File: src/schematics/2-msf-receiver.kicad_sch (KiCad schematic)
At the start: 3 parts

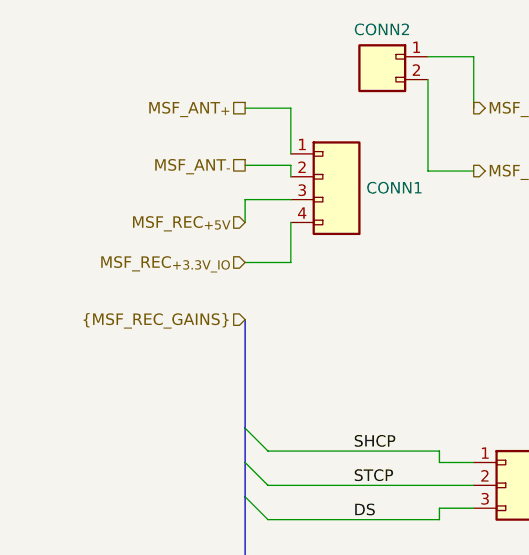
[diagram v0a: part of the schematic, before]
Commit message: Elaboration of the top-level schematicd.
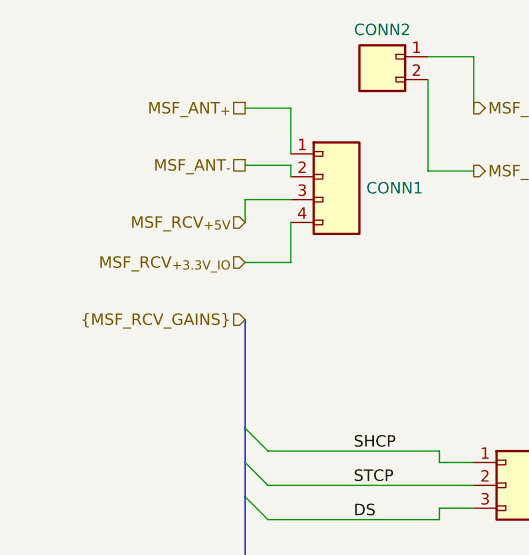
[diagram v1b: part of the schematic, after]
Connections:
- net MSF_REC_{+3.3V_IO} renamed MSF_RCV_{+3.3V_IO}
- net MSF_REC_{+5V} renamed MSF_RCV_{+5V}
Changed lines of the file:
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@@
     (company "Pete Restall <pete@restall.net>")
   )
-  (bus_alias "MSF_REC_GAINS" (members "SHCP" "STCP" "DS"))
+  (bus_alias "MSF_RCV_GAINS" (members "SHCP" "STCP" "DS"))
   (bus_entry (at 38.1 93.98) (size 2.54 2.54)
     (stroke (width 0) (type default))
@@
     (effects (font (size 1.27 1.27)) (justify right))
   )
-  (hierarchical_label "MSF_REC_{+5V}" (shape input) (at 38.1 63.5 180) (fields_autoplaced)
+  (hierarchical_label "MSF_RCV_{+5V}" (shape input) (at 38.1 63.5 180) (fields_autoplaced)
     (effects (font (size 1.27 1.27)) (justify right))
   )
-  (hierarchical_label "MSF_REC_{+3.3V_IO}" (shape input) (at 38.1 67.945 180) (fields_autoplaced)
+  (hierarchical_label "MSF_RCV_{+3.3V_IO}" (shape input) (at 38.1 67.945 180) (fields_autoplaced)
     (effects (font (size 1.27 1.27)) (justify right))
   )
@@
     (effects (font (size 1.27 1.27)) (justify left))
   )
-  (hierarchical_label "{MSF_REC_GAINS}" (shape input) (at 38.1 74.295 180) (fields_autoplaced)
+  (hierarchical_label "{MSF_RCV_GAINS}" (shape input) (at 38.1 74.295 180) (fields_autoplaced)
     (effects (font (size 1.27 1.27)) (justify right))
   )

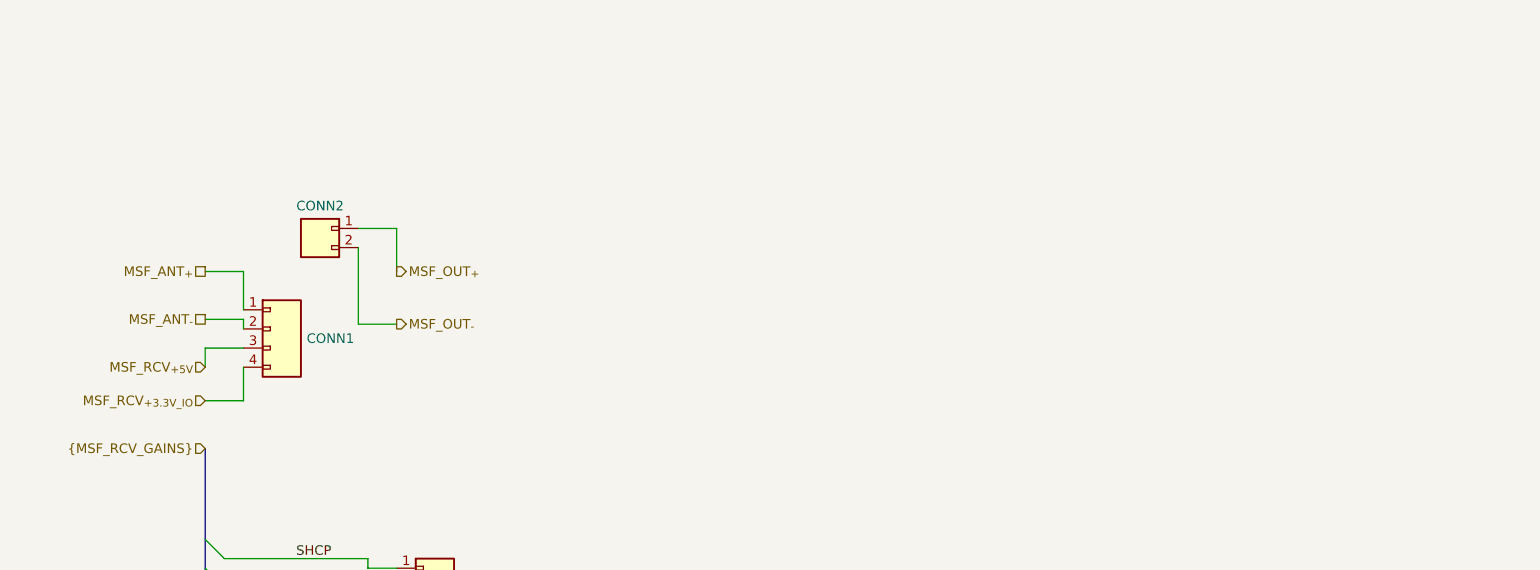
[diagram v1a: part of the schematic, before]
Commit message: Further elaboration of the design and schematics, mainly power supply calculations.
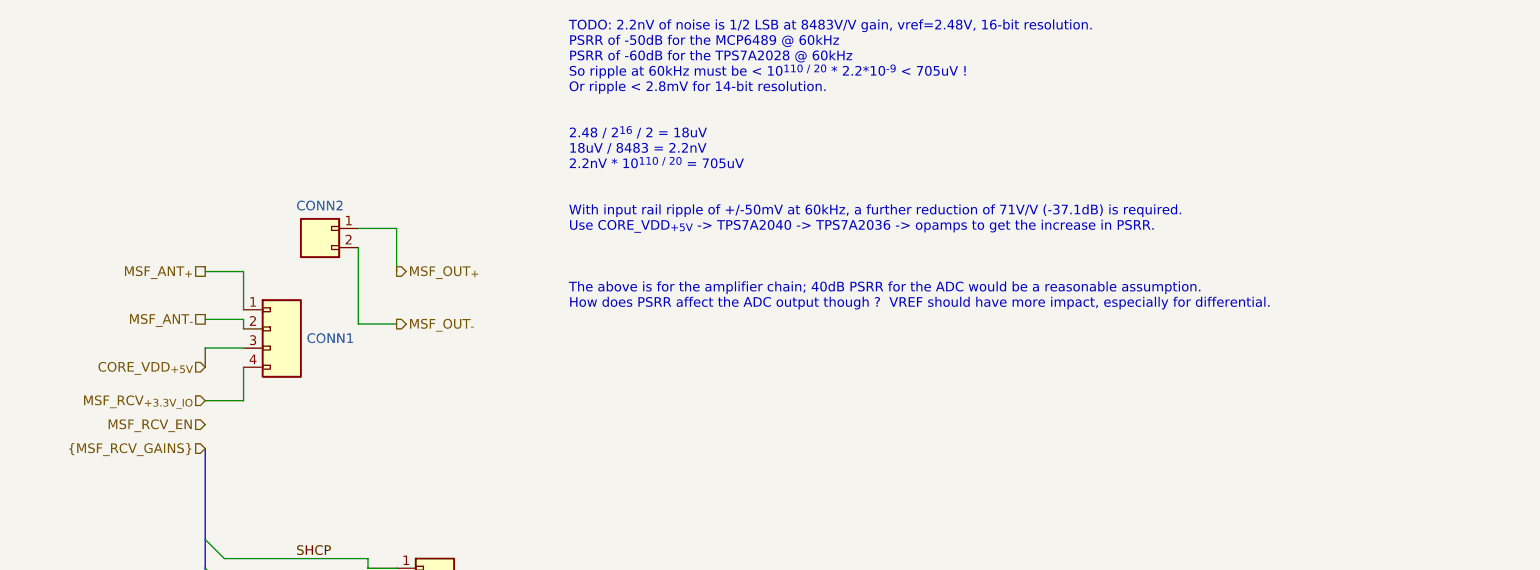
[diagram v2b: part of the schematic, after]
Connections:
- net MSF_RCV_{+5V} renamed CORE_VDD_{+5V}
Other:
- note added: "TODO: 2.2nV of noise is 1/2 LSB at 8483V/V gain, vref=2.48V, 16-bit resolution. PSRR of -50dB for the MCP6489 @ 60kHz PSRR of -60dB for the TPS7A2028 @ 60kHz So ripple at 60kHz must be < 10^{110 / 20} * 2.2*10^{-9} < 705uV ! Or ripple < 2.8mV for 14-bit resolution. 2.48 / 2^{16} / 2 = 18uV 18uV / 8483 = 2.2nV 2.2nV * 10^{110 / 20} = 705uV With input rail ripple of +/-50mV at 60kHz, a further redu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"
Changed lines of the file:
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@@
     (stroke (width 0) (type default))
+  )
+  (text "TODO: 2.2nV of noise is 1/2 LSB at 8483V/V gain, vref=2.48V, 16-bit resolution.\nPSRR of -50dB for the MCP6489 @ 60kHz\nPSRR of -60dB for the TPS7A2028 @ 60kHz\nSo ripple at 60kHz must be < 10^{110 / 20} * 2.2*10^{-9} < 705uV !\nOr ripple < 2.8mV for 14-bit resolution.\n\n\n2.48 / 2^{16} / 2 = 18uV\n18uV / 8483 = 2.2nV\n2.2nV * 10^{110 / 20} = 705uV\n\n\nWith input rail ripple of +/-50mV at 60kHz, a further reduction of 71V/V (-37.1dB) is required.\nUse CORE_VDD_{+5V} -> TPS7A2040 -> TPS7A2036 -> opamps to get the increase in PSRR.\n\n\n\nThe above is for the amplifier chain; 40dB PSRR for the ADC would be a reasonable assumption.\nHow does PSRR affect the ADC output though ?  VREF should have more impact, especially for differential."
+    (at 86.36 55.88 0)
+    (effects (font (size 1.27 1.27)) (justify left bottom))
   )
   (label "STCP" (at 50.165 92.71 0) (fields_autoplaced)
@@
     (effects (font (size 1.27 1.27)) (justify right))
   )
-  (hierarchical_label "MSF_RCV_{+5V}" (shape input) (at 38.1 63.5 180) (fields_autoplaced)
+  (hierarchical_label "CORE_VDD_{+5V}" (shape input) (at 38.1 63.5 180) (fields_autoplaced)
     (effects (font (size 1.27 1.27)) (justify right))
   )
@@
     (effects (font (size 1.27 1.27)) (justify right))
   )
+  (hierarchical_label "MSF_RCV_EN" (shape input) (at 38.1 71.12 180) (fields_autoplaced)
+    (effects (font (size 1.27 1.27)) (justify right))
+  )

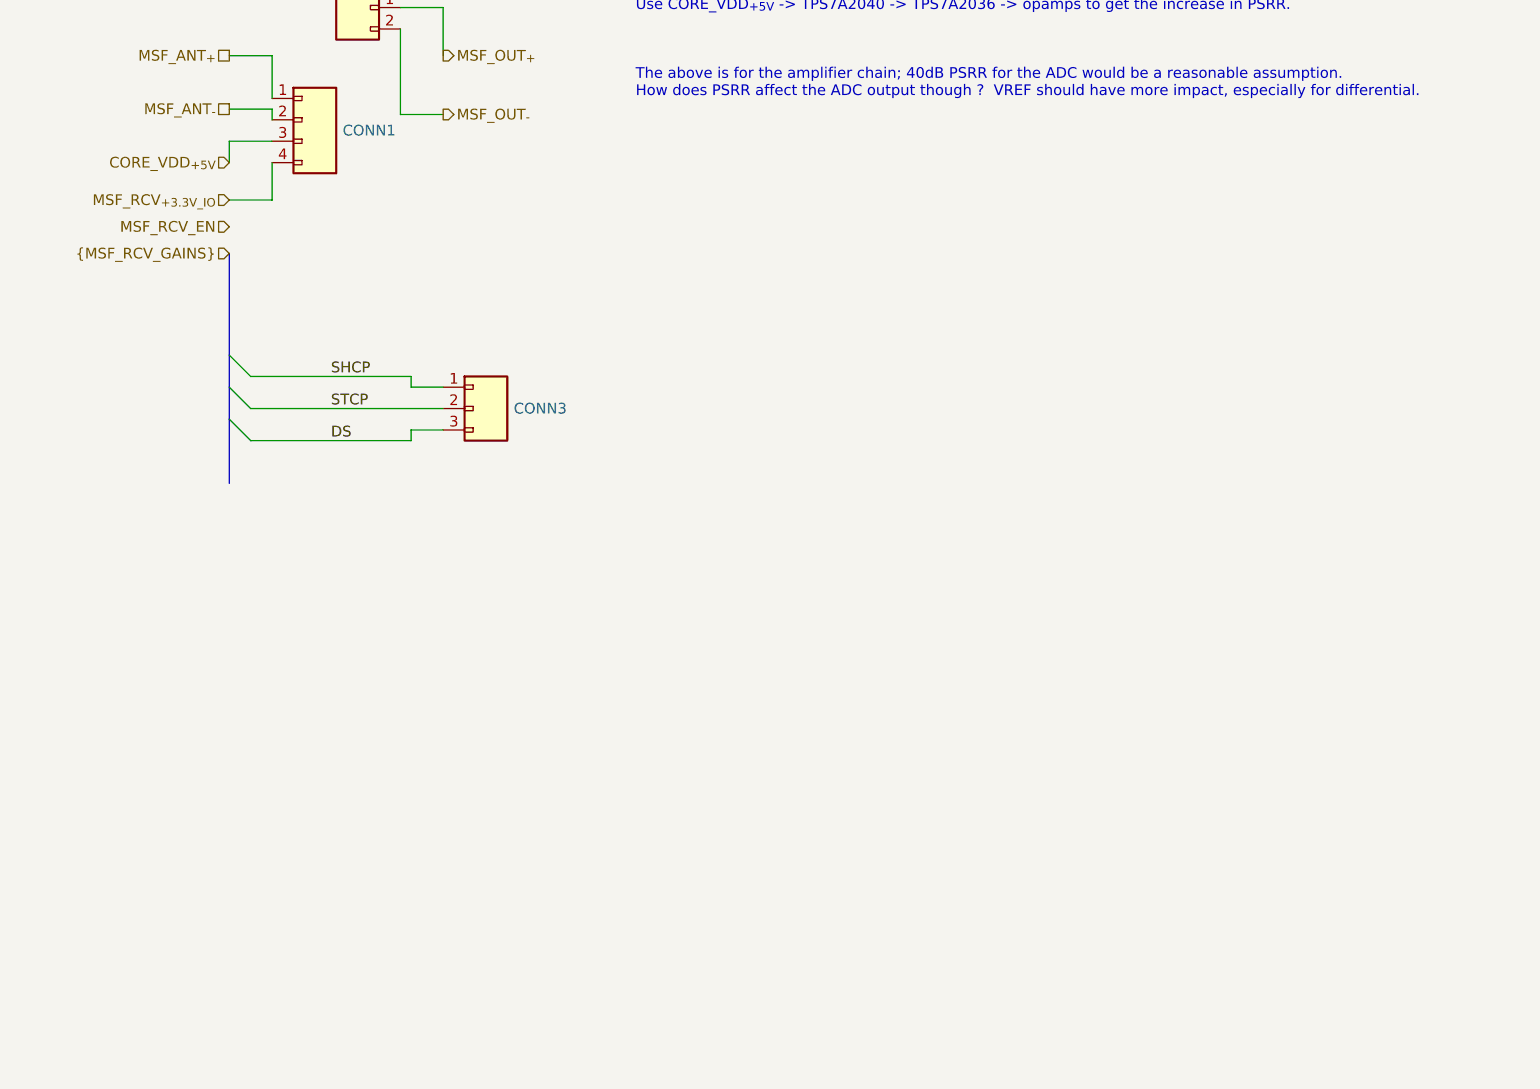
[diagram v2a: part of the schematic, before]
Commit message: Further elaboration of the USB / Power schematic.
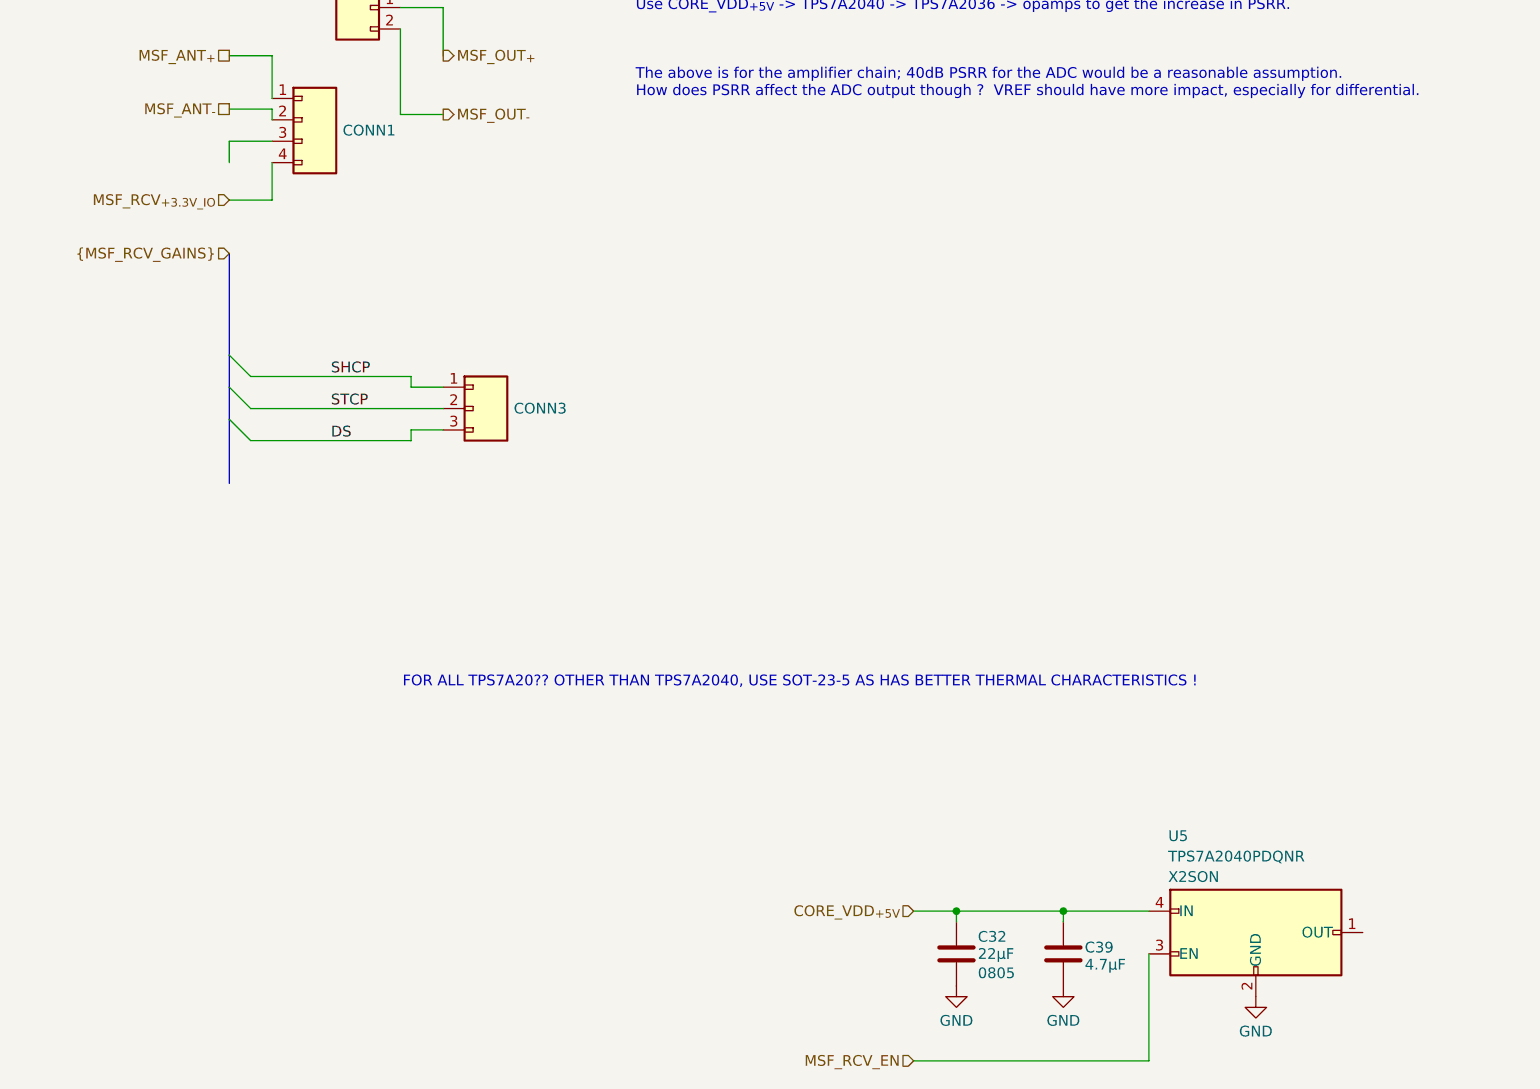
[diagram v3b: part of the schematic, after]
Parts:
- added C32: 22μF, restall-generic-capacitors:unpolarised-nominal-0805-2012, symbol restall-generic-capacitors:capacitor-unpolarised
- added C39: 4.7μF, restall-generic-capacitors:unpolarised-nominal-0402-1005, symbol restall-generic-capacitors:capacitor-unpolarised
- added U5: TPS7A2040PDQNR, restall-manufacturer-ti:X2SON4-1x1mm-0.65mm-expad-0.48x0.48mm, symbol restall-manufacturer-ti:TPS7A20??PDQNR
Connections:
- net CORE_VDD_{+5V}: now also C32.1, C39.1, U5.4 (IN); no longer CONN1.3 (P3)
- net MSF_RCV_EN: now also U5.3 (EN)
- new net GND: C32.2, C39.2, U5.2 (GND), U5.5 (GND)
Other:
- note added: "FOR ALL TPS7A20?? OTHER THAN TPS7A2040, USE SOT-23-5 AS HAS BETTER THERMAL CHARACTERISTICS !"

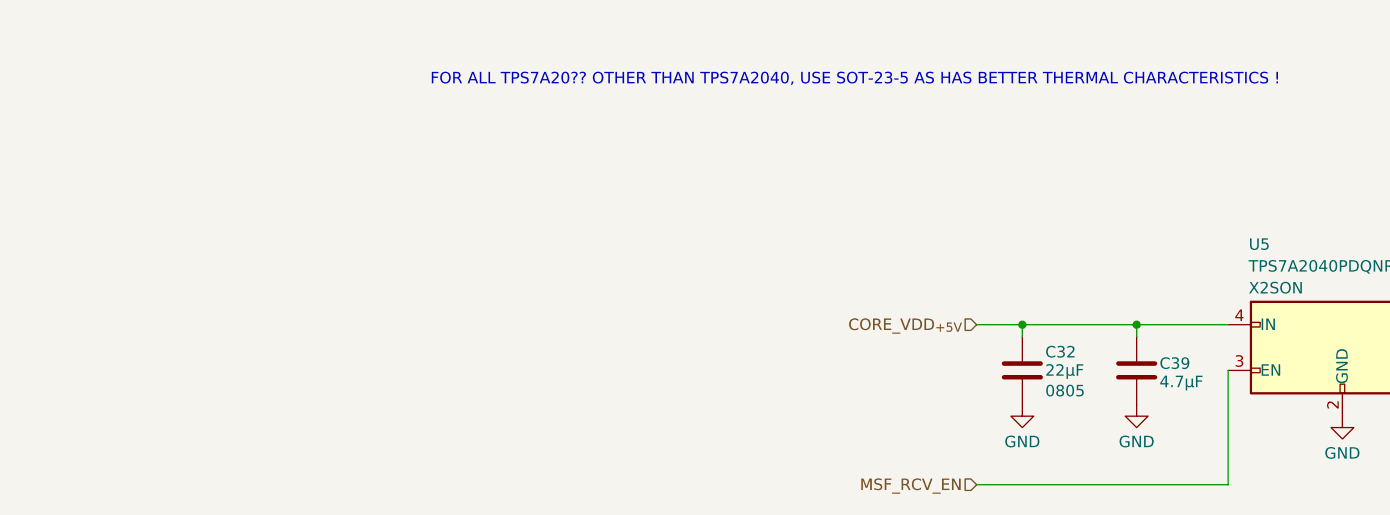
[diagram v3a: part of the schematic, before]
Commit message: Further elaboration of the USB / power module schematics.
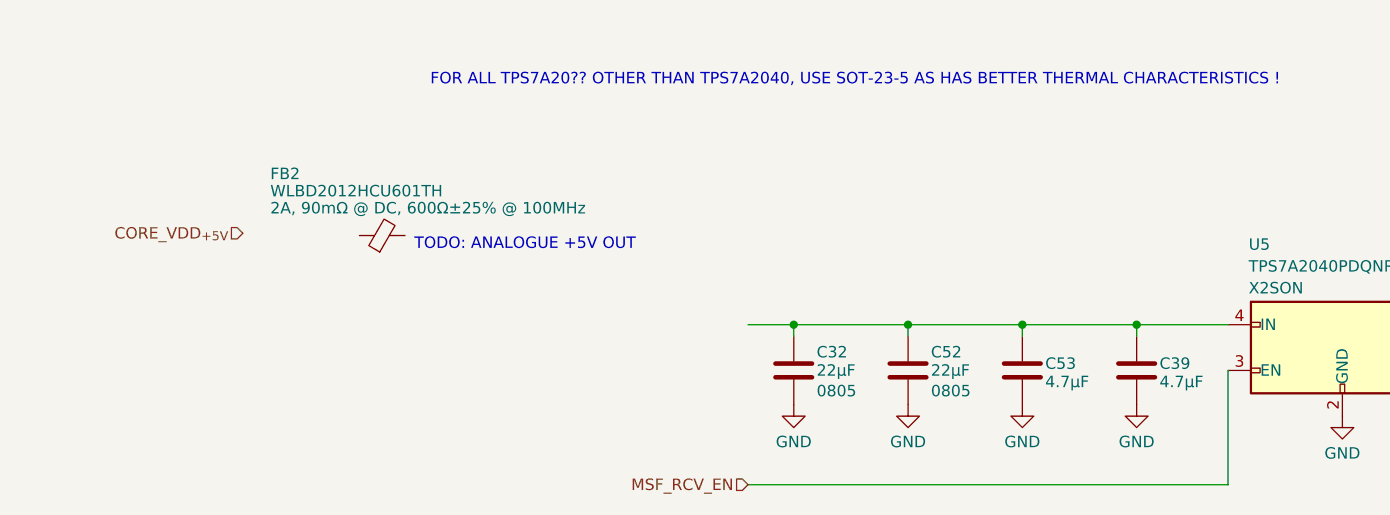
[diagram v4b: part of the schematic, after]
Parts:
- added C52: 22μF, restall-generic-capacitors:unpolarised-nominal-0805-2012, symbol restall-generic-capacitors:capacitor-unpolarised
- added C53: 4.7μF, restall-generic-capacitors:unpolarised-nominal-0402-1005, symbol restall-generic-capacitors:capacitor-unpolarised
- added FB2: WLBD2012HCU601TH, restall-manufacturer-walsin:WLBD2012, symbol restall-manufacturer-walsin:WLBD2012HCU601TH
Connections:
- net CORE_VDD_{+5V}: no longer C32.1, C39.1, U5.4 (IN)
- net GND: now also C52.2, C53.2
- new net: C32.1, C39.1, C52.1, C53.1, U5.4 (IN)
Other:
- note added: "TODO: ANALOGUE +5V OUT"
- moved on the sheet: C32

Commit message: Started to elaborate the MSF front-end schematic.
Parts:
- added C24, C25, C28, C29: 4.7μF, restall-generic-capacitors:unpolarised-nominal-0402-1005, symbol restall-generic-capacitors:capacitor-unpolarised
- added C26, C27: 22μF, restall-generic-capacitors:unpolarised-nominal-0805-2012, symbol restall-generic-capacitors:capacitor-unpolarised
- added U2: TPS7A2036PDBVR, restall-manufacturer-ti:TPS7A20??PDBVR, symbol restall-manufacturer-ti:TPS7A20??PDBVR
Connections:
- net CORE_VDD_{+5V}: now also FB2.1 (P1)
- net GND: now also C24.2, C25.2, C26.2, C27.2, C28.2, C29.2, U2.2 (GND)
- net at C32.1, C39.1, C52.1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: now also FB2.2 (P2)
- net at U5.1 (OUT): now also C24.1, C25.1, C26.1, C27.1, C28.1, C29.1, U2.1 (IN), U2.3 (EN)
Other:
- note added: "PSRR of -110dB @ 60kHz for cascaded TPS7A2040 and TPS7A2036, in addition to the MCP6489's -50dB gives -160dB total in-band PSRR PSRR of -70dB @ 1MHz for cascaded TPS7A2040 and TPS7A2036, in addition to the MCP6489's -25dB gives -95dB total PSRR up to ADC sampling frequency gives a theoretical 15.5 bits of resolution"
- note added: "TODO: VERIFY THERMAL PERFORMANCE OF TPS7A20xx AT MAXIMUM CURRENT AND VOLTAGE DROPS"
- note removed: "TODO: ANALOGUE +5V OUT"
- moved on the sheet: FB2

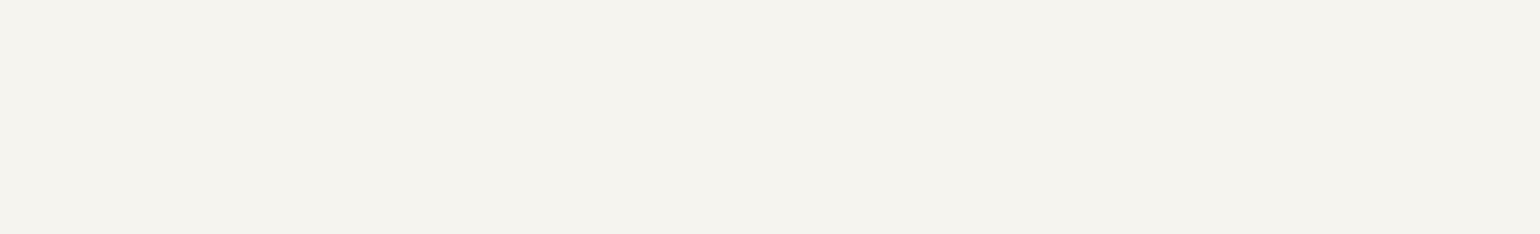
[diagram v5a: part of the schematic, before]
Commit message: Added a TODO as a reminder not to forget about discharging the reference rails on power-down.
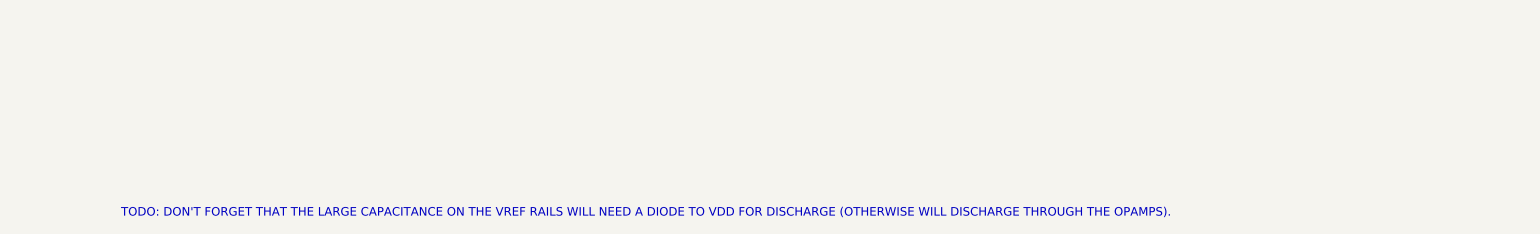
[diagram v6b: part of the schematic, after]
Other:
- note added: "TODO: DON'T FORGET THAT THE LARGE CAPACITANCE ON THE VREF RAILS WILL NEED A DIODE TO VDD FOR DISCHARGE (OTHERWISE WILL DISCHARGE THROUGH THE OPAMPS)."
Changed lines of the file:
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@@
+    (effects (font (size 1.27 1.27)) (justify left bottom))
+  )
+  (text "TODO: DON'T FORGET THAT THE LARGE CAPACITANCE ON THE VREF RAILS WILL NEED A DIODE TO VDD FOR DISCHARGE (OTHERWISE WILL DISCHARGE THROUGH THE OPAMPS)."
+    (at 100.584 243.586 0)
     (effects (font (size 1.27 1.27)) (justify left bottom))
   )
